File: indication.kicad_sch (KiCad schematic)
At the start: 0 parts

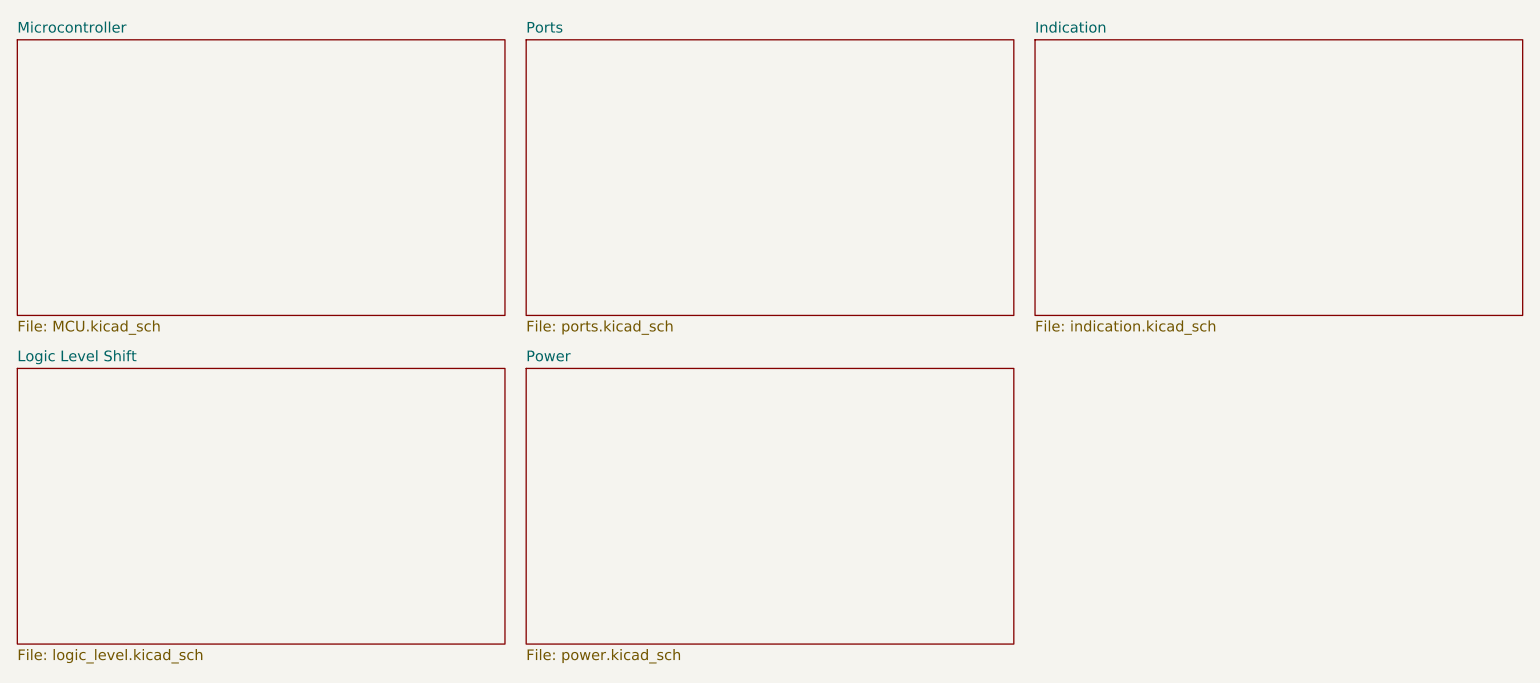
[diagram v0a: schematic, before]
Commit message: Break up schematic into hierarchical sheets
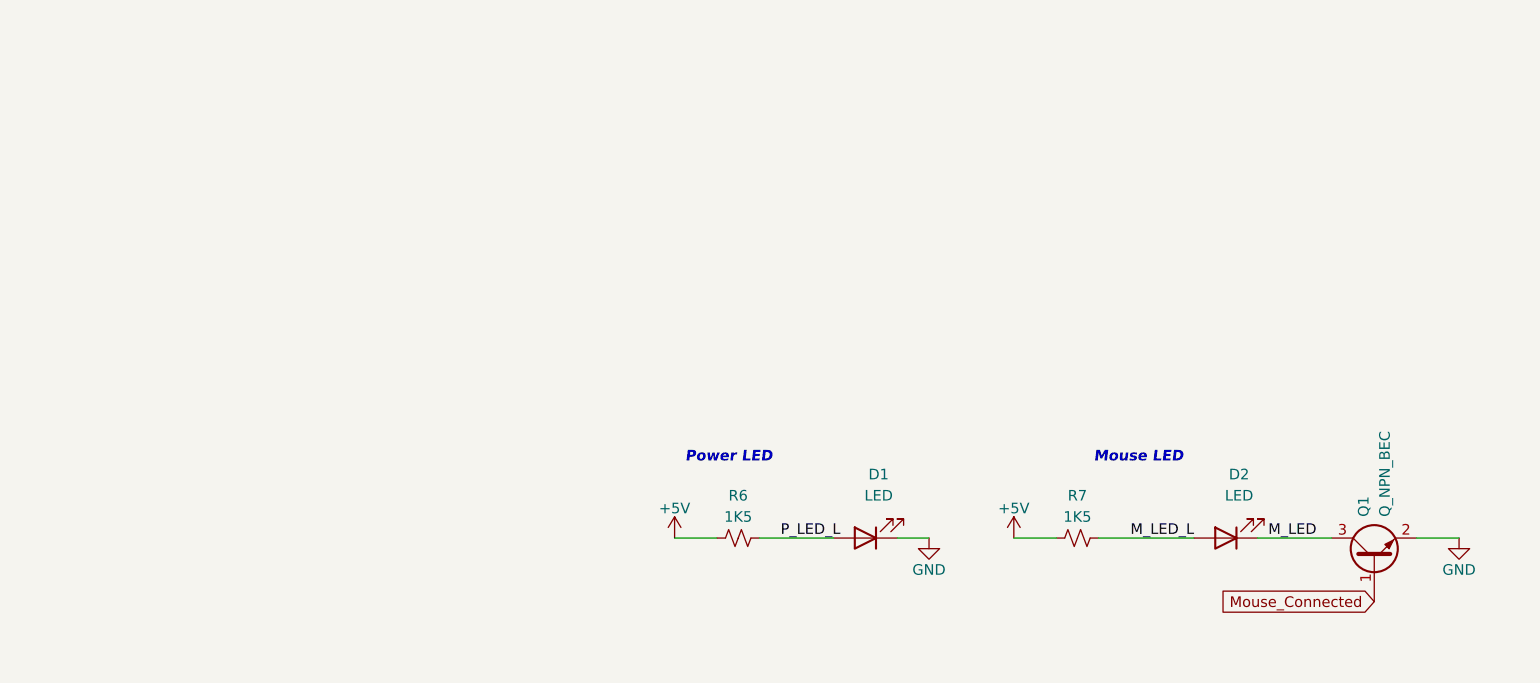
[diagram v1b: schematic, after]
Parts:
- added D1, D2: LED, LED_SMD:LED_0603_1608Metric, symbol Device:LED
- added Q1: Q_NPN_BEC, Package_TO_SOT_SMD:SOT-23-3, symbol Device:Q_NPN_BEC
- added R6, R7: 1K5, Resistor_SMD:R_0402_1005Metric, symbol Device:R_Small_US
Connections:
- new net +5V: R6.1, R7.1
- new net GND: D1.1 (K), Q1.2 (E)
- new net M_LED: D2.1 (K), Q1.3 (C)
- new net M_LED_L: D2.2 (A), R7.2
- new net Mouse_Connected: Q1.1 (B)
- new net P_LED_L: D1.2 (A), R6.2
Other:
- removed sheet Indication
- removed sheet Logic Level Shift
- removed sheet Microcontroller
- removed sheet Ports
- removed sheet Power
- note added: "Mouse LED"
- note added: "Power LED"
